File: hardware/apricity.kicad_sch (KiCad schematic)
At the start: 2 parts

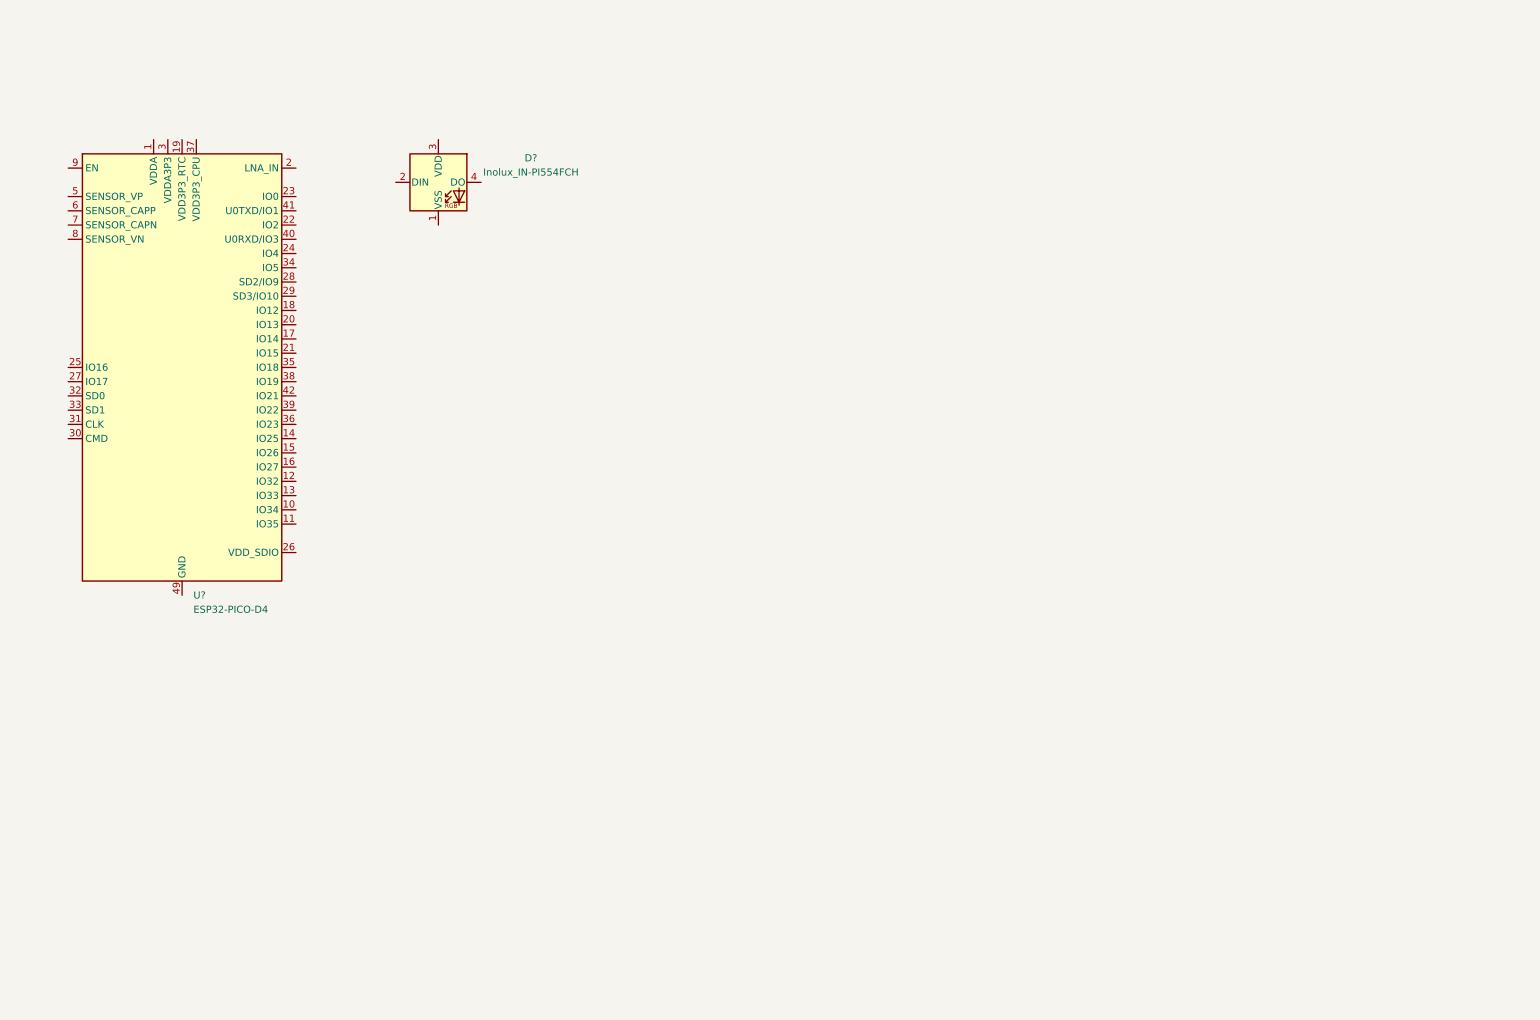
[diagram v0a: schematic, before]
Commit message: Prototype ESP8266-based version
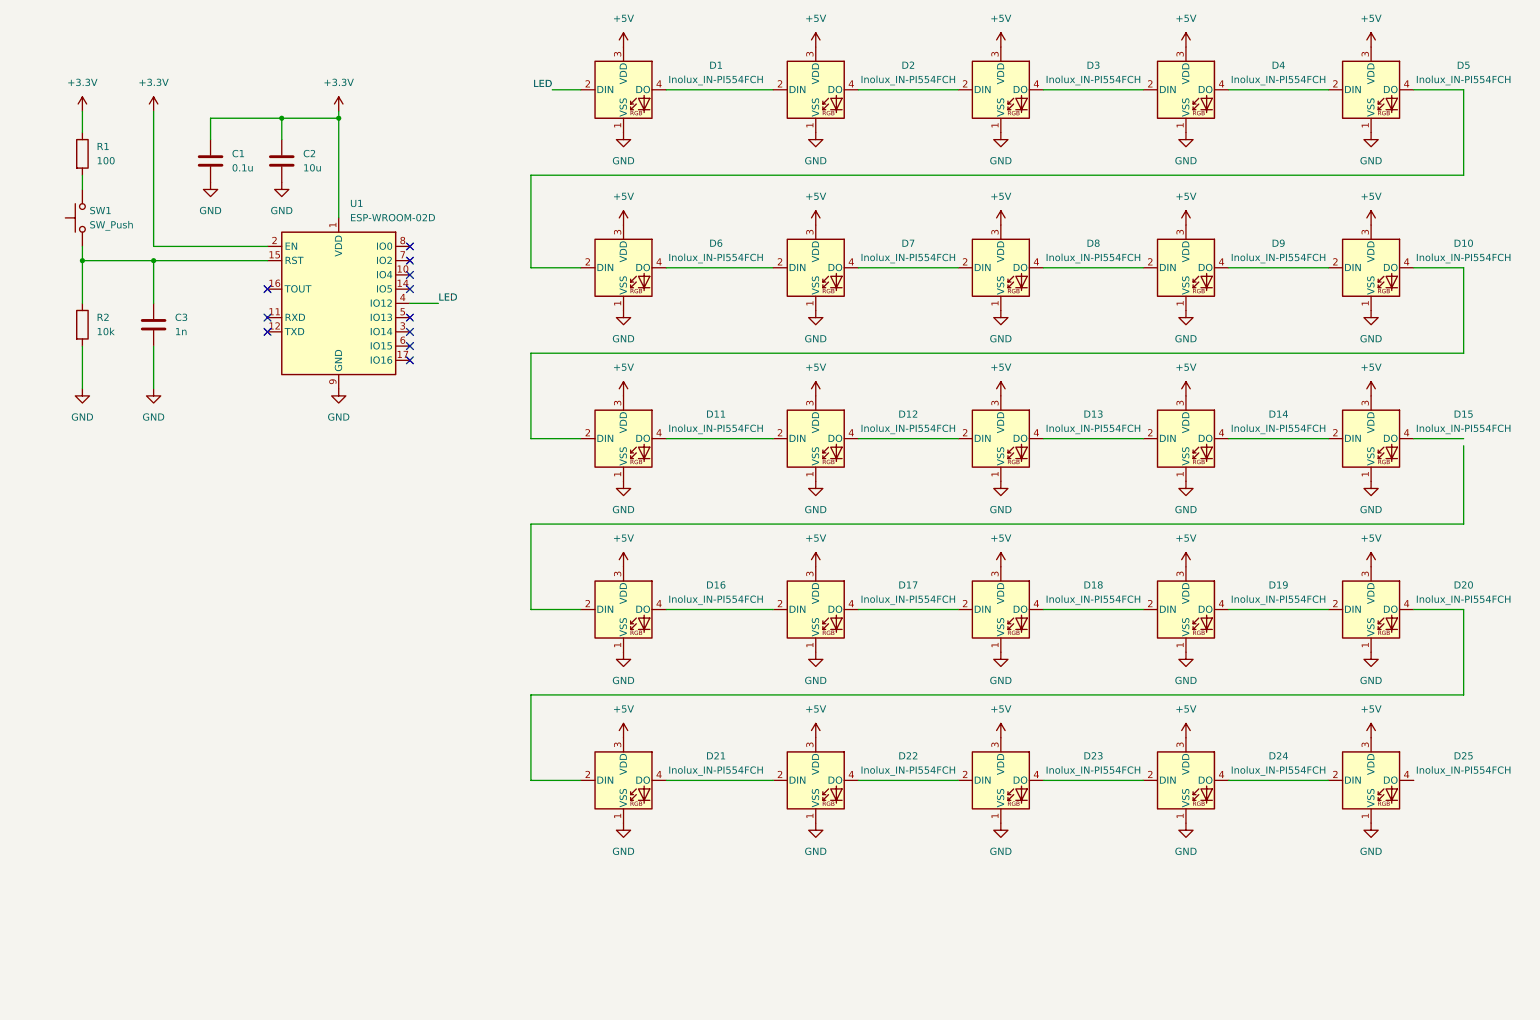
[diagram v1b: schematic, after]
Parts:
- removed U?: ESP32-PICO-D4, Package_DFN_QFN:QFN-48-1EP_7x7mm_P0.5mm_EP5.3x5.3mm, symbol RF_Module:ESP32-PICO-D4
- added C1: 0.1u, symbol Device:C
- added C2: 10u, symbol Device:C
- added C3: 1n, symbol Device:C
- added D1, D10, D11, D12, D13, D14, D15, D16, D17, D18, D19, D20, D21, D22, D23, D24, D25, D3, D4, D5, D6, D7, D8, D9: Inolux_IN-PI554FCH, LED_SMD:LED_Inolux_IN-PI554FCH_PLCC4_5.0x5.0mm_P3.2mm, symbol LED:Inolux_IN-PI554FCH
- added R1: 100, Resistor_SMD:R_0805_2012Metric, symbol Device:R
- added R2: 10k, Resistor_SMD:R_0805_2012Metric, symbol Device:R
- added SW1: SW_Push, symbol Switch:SW_Push
- added U1: ESP-WROOM-02D, RF_Module:ESP-WROOM-02, symbol RF_Module:ESP-WROOM-02
- gave numbers to parts that had none: 1
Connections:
- net GND: now reaches D2.1 (VSS)
- net GND: now also C1.2, C2.2, C3.2, D1.1 (VSS), D10.1 (VSS), D11.1 (VSS), D12.1 (VSS), D13.1 (VSS), D14.1 (VSS), D15.1 (VSS), D16.1 (VSS), D17.1 (VSS), D18.1 (VSS), D19.1 (VSS), D20.1 (VSS), D21.1 (VSS), D22.1 (VSS), D23.1 (VSS), D24.1 (VSS), D25.1 (VSS), D3.1 (VSS), D4.1 (VSS), D5.1 (VSS), D6.1 (VSS), D7.1 (VSS), D8.1 (VSS), D9.1 (VSS), R2.2, U1.13 (GND), U1.18 (GND), U1.19 (GND), U1.9 (GND)
- net at D2.2 (DIN): now also D1.4 (DO)
- net +5V: now reaches D2.3 (VDD)
- net +5V: now also D1.3 (VDD), D10.3 (VDD), D11.3 (VDD), D12.3 (VDD), D13.3 (VDD), D14.3 (VDD), D15.3 (VDD), D16.3 (VDD), D17.3 (VDD), D18.3 (VDD), D19.3 (VDD), D20.3 (VDD), D21.3 (VDD), D22.3 (VDD), D23.3 (VDD), D24.3 (VDD), D25.3 (VDD), D3.3 (VDD), D4.3 (VDD), D5.3 (VDD), D6.3 (VDD), D7.3 (VDD), D8.3 (VDD), D9.3 (VDD)
- net at D2.4 (DO): now also D3.2 (DIN)
- new net: D16.4 (DO), D17.2 (DIN)
- new net: D17.4 (DO), D18.2 (DIN)
- new net: C3.1, R2.1, SW1.1, U1.15 (RST)
- new net: D22.4 (DO), D23.2 (DIN)
- new net: D23.4 (DO), D24.2 (DIN)
- new net: R1.2, SW1.2
- new net: D13.4 (DO), D14.2 (DIN)
- new net: D14.4 (DO), D15.2 (DIN)
- new net: D24.4 (DO), D25.2 (DIN)
- new net: D12.4 (DO), D13.2 (DIN)
- new net: D18.4 (DO), D19.2 (DIN)
- new net: D10.4 (DO), D11.2 (DIN)
- new net: D11.4 (DO), D12.2 (DIN)
- new net: D19.4 (DO), D20.2 (DIN)
- new net: D3.4 (DO), D4.2 (DIN)
- new net: D4.4 (DO), D5.2 (DIN)
- new net: D7.4 (DO), D8.2 (DIN)
- new net: D8.4 (DO), D9.2 (DIN)
- new net: D6.4 (DO), D7.2 (DIN)
- new net: D20.4 (DO), D21.2 (DIN)
- new net: D5.4 (DO), D6.2 (DIN)
- new net: D10.2 (DIN), D9.4 (DO)
- new net: D21.4 (DO), D22.2 (DIN)
- new net +3.3V: C1.1, C2.1, R1.1, U1.1 (VDD), U1.2 (EN)
- new net LED: D1.2 (DIN), U1.4 (IO12)
- no-connect marks 0 -> 11
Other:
- moved on the sheet: D2

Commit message: lay down prototype circular array
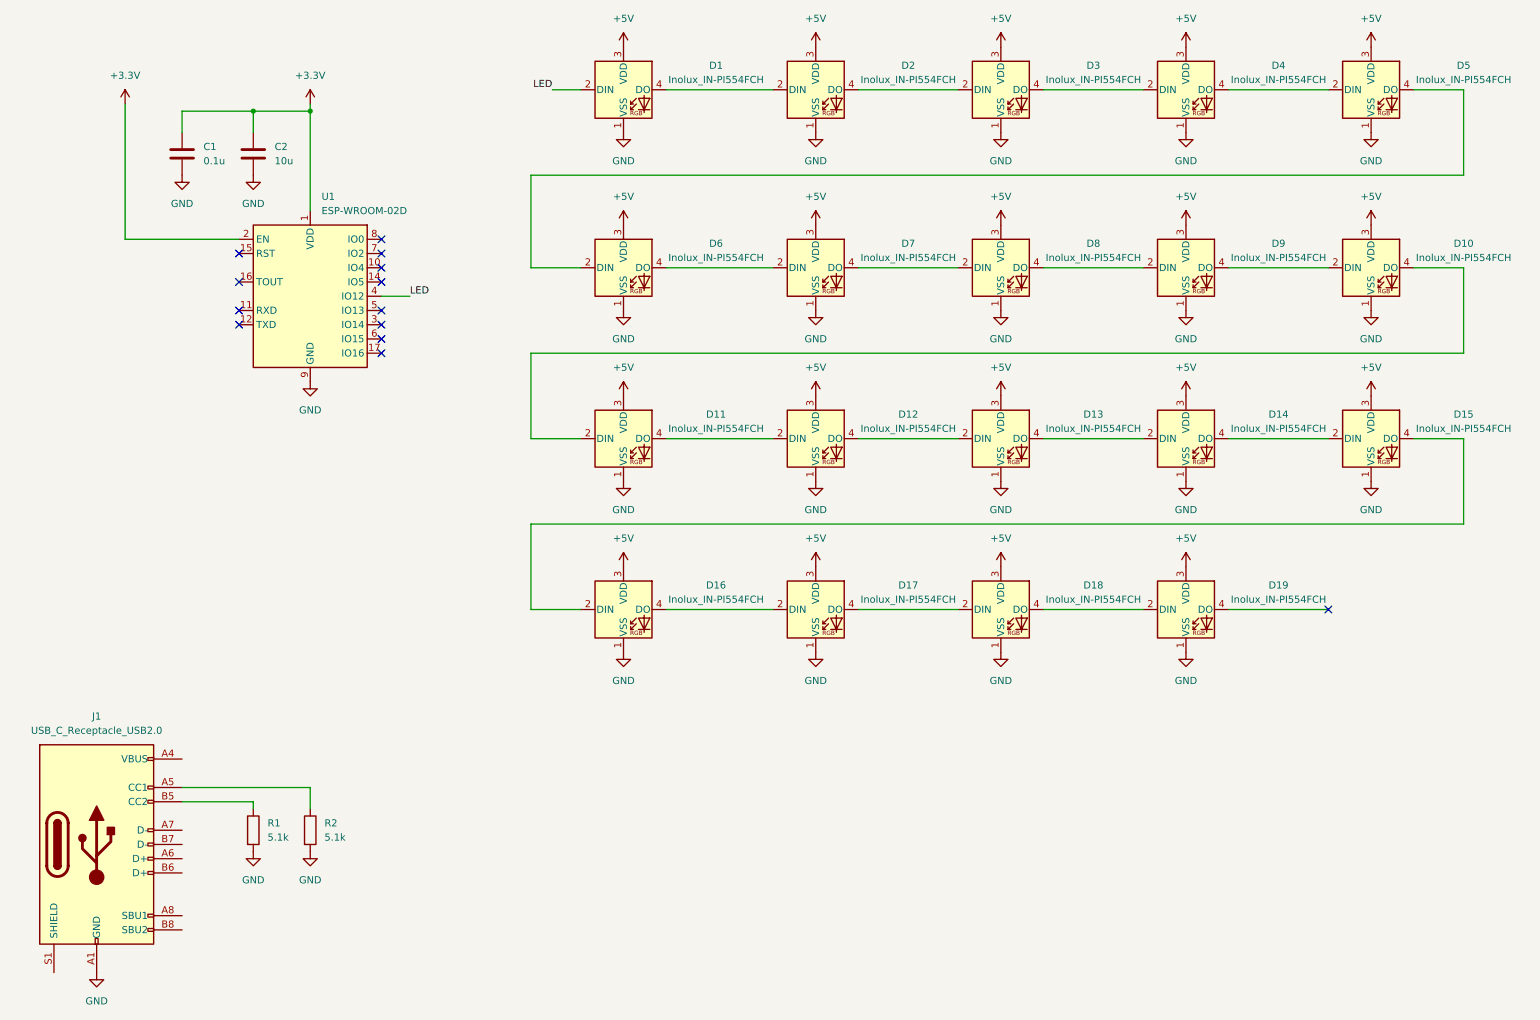
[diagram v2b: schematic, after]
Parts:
- removed C3: 1n, symbol Device:C
- removed D20, D21, D22, D23, D24, D25: Inolux_IN-PI554FCH, LED_SMD:LED_Inolux_IN-PI554FCH_PLCC4_5.0x5.0mm_P3.2mm, symbol LED:Inolux_IN-PI554FCH
- removed SW1: SW_Push, symbol Switch:SW_Push
- added J1: USB_C_Receptacle_USB2.0, Connector_USB:USB_C_Receptacle_GCT_USB4085, symbol Connector:USB_C_Receptacle_USB2.0
- R1: value 100 -> 5.1k; footprint Resistor_SMD:R_0805_2012Metric -> (none)
- R2: value 10k -> 5.1k; footprint Resistor_SMD:R_0805_2012Metric -> (none)
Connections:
- net +3.3V: no longer R1.1
- net GND: now also R1.2, J1.A1 (GND), J1.A12 (GND), J1.B1 (GND), J1.B12 (GND)
- net at U1.15 (RST): no longer R2.1
- net at D15.4 (DO): now also D16.2 (DIN)
- new net: J1.B5 (CC2), R1.1
- new net: J1.A5 (CC1), R2.1
- new net: J1.A4 (VBUS), J1.A9 (VBUS), J1.B4 (VBUS), J1.B9 (VBUS)
- no-connect marks 11 -> 13
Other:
- moved on the sheet: C1, C2, U1

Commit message: Annotate schematic and add power components
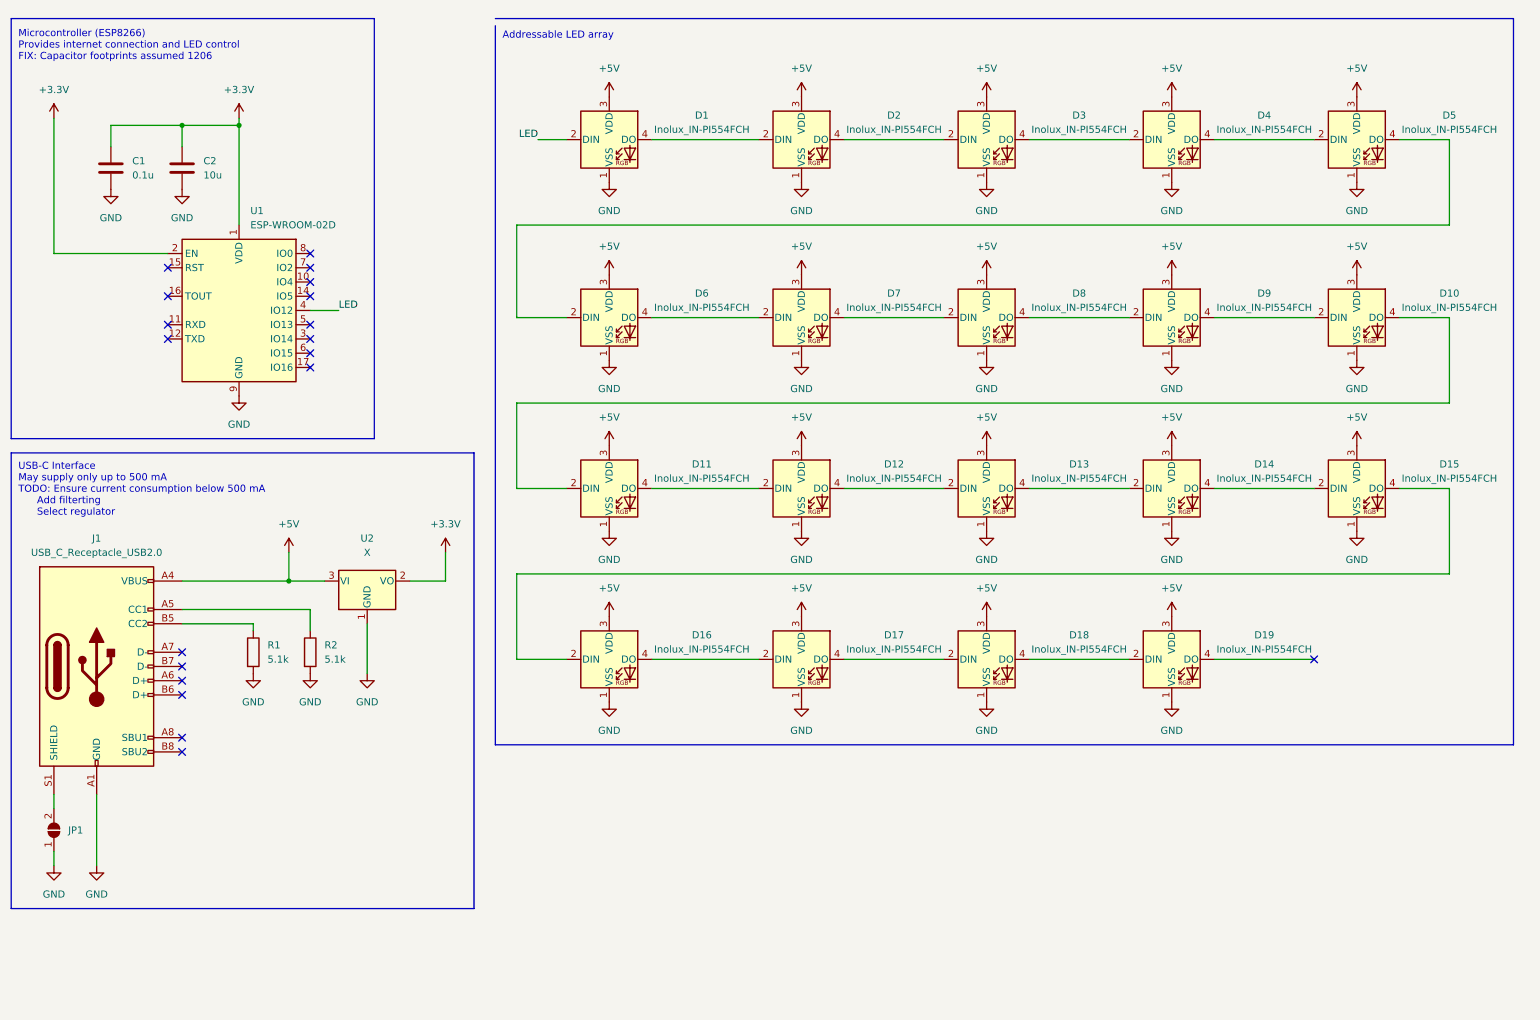
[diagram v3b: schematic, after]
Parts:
- added JP1: SolderJumper_2_Open, symbol Jumper:SolderJumper_2_Open
- added U2: X, Package_TO_SOT_SMD:TSOT-23_HandSoldering, symbol Regulator_Linear:AMS1117-3.3
- C1, C2: footprint (none) -> Capacitor_SMD:C_1206_3216Metric
- R1, R2: footprint (none) -> Resistor_SMD:R_0805_2012Metric
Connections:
- net +3.3V: now also U2.2 (VO)
- net +5V: now also J1.A4 (VBUS), J1.A9 (VBUS), J1.B4 (VBUS), J1.B9 (VBUS), U2.3 (VI)
- net GND: now also JP1.1 (A), U2.1 (GND)
- net at J1.S1 (SHIELD): now also JP1.2 (B)
- no-connect marks 13 -> 19
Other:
- note added: "Addressable LED array"
- note added: "Microcontroller (ESP8266) Provides internet connection and LED control FIX: Capacitor footprints assumed 1206"
- note added: "USB-C Interface May supply only up to 500 mA TODO: Ensure current consumption below 500 mA Add filterting Select regulator"
- moved on the sheet: C1, C2, D1, D10, D11, D12, D13, D15, D16, D17, D18, D19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

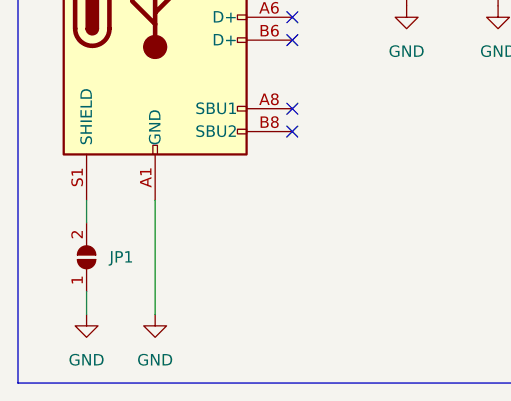
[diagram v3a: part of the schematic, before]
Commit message: layout power components on pcb
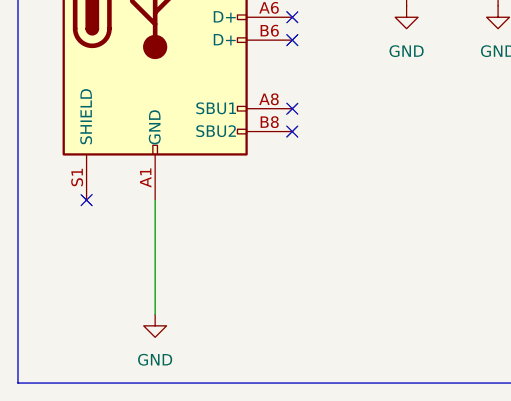
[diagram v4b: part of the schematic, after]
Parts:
- removed JP1: SolderJumper_2_Open, symbol Jumper:SolderJumper_2_Open
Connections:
- no-connect marks 19 -> 20
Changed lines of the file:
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@@
   )
   (no_connect (at 45.72 143.51))
+  (no_connect (at 22.86 153.67))
   (no_connect (at 68.58 77.47))
   (no_connect (at 68.58 64.77))
@@
   (no_connect (at 45.72 135.89))
   (no_connect (at 68.58 69.85))
-  (wire (pts (xy 22.86 163.83) (xy 22.86 166.37))
-    (stroke (width 0) (type default) (color 0 0 0 0))
-  )
   (wire (pts (xy 229.87 68.58) (xy 247.65 68.58))
     (stroke (width 0) (type default) (color 0 0 0 0))
@@
   )
   (wire (pts (xy 105.41 129.54) (xy 114.3 129.54))
-    (stroke (width 0) (type default) (color 0 0 0 0))
-  )
-  (wire (pts (xy 22.86 153.67) (xy 22.86 156.21))
     (stroke (width 0) (type default) (color 0 0 0 0))
   )
@@
     (pin "1")
   )
-  (symbol (lib_id "power:GND") (at 22.86 166.37 0) (unit 1)
-    (in_bom yes) (on_board yes) (fields_autoplaced)
-    (property "Reference" "#PWR049" (id 0) (at 22.86 172.72 0)
-      (effects (font (size 1.27 1.27)) hide)
-    )
-    (property "Value" "GND" (id 1) (at 22.86 171.45 0))
-    (property "Footprint" "" (id 2) (at 22.86 166.37 0)
-      (effects (font (size 1.27 1.27)) hide)
-    )
-    (property "Datasheet" "" (id 3) (at 22.86 166.37 0)
-      (effects (font (size 1.27 1.27)) hide)
-    )
-    (pin "1")
-  )
   (symbol (lib_id "power:+5V") (at 156.21 29.21 0) (unit 1)
     (in_bom yes) (on_board yes) (fields_autoplaced)
@@
     )
     (pin "1")
-  )
-  (symbol (lib_id "Jumper:SolderJumper_2_Open") (at 22.86 160.02 90) (unit 1)
-    (in_bom yes) (on_board yes) (fields_autoplaced)
-    (property "Reference" "JP1" (id 0) (at 25.4 160.0199 90)
-      (effects (font (size 1.27 1.27)) (justify right))
-    )
-    (property "Value" "SolderJumper_2_Open" (id 1) (at 25.4 161.2899 90)
-      (effects (font (size 1.27 1.27)) (justify right) hide)
-    )
-    (property "Footprint" "" (id 2) (at 22.86 160.02 0)
-      (effects (font (size 1.27 1.27)) hide)
-    )
-    (property "Datasheet" "~" (id 3) (at 22.86 160.02 0)
-      (effects (font (size 1.27 1.27)) hide)
-    )
-    (pin "1")
-    (pin "2")
   )
   (symbol (lib_id "power:+5V") (at 156.21 121.92 0) (unit 1)
@@
       (reference "#PWR048") (unit 1) (value "GND") (footprint "")
     )
-    (path "/8088c610-75e5-445a-810f-db520c1a5a91"
-      (reference "#PWR049") (unit 1) (value "GND") (footprint "")
-    )
     (path "/e2c4a6fe-1e37-465a-8920-4c4fc7446705"
       (reference "#PWR050") (unit 1) (value "GND") (footprint "")
@@
       (reference "J1") (unit 1) (value "USB_C_Receptacle_USB2.0") (footprint "Connector_USB:USB_C_Receptacle_GCT_USB4085")
     )
-    (path "/91d1ca4e-50dd-4a51-8711-673ec4693390"
-      (reference "JP1") (unit 1) (value "SolderJumper_2_Open") (footprint "")
-    )
     (path "/0d05b2dd-0847-494b-a812-c82d7fd47262"

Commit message: Play with power planes
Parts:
- J1: footprint Connector_USB:USB_C_Receptacle_GCT_USB4085 -> Connector_USB:USB_C_Receptacle_XKB_U262-16XN-4BVC11
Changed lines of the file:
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@@
     (property "Reference" "J1" (id 0) (at 30.48 107.95 0))
     (property "Value" "USB_C_Receptacle_USB2.0" (id 1) (at 30.48 110.49 0))
-    (property "Footprint" "Connector_USB:USB_C_Receptacle_GCT_USB4085" (id 2) (at 34.29 130.81 0)
+    (property "Footprint" "Connector_USB:USB_C_Receptacle_XKB_U262-16XN-4BVC11" (id 2) (at 34.29 130.81 0)
       (effects (font (size 1.27 1.27)) hide)
     )
@@
     )
     (path "/efec80d5-3b93-449b-967c-e6308c2f145f"
-      (reference "J1") (unit 1) (value "USB_C_Receptacle_USB2.0") (footprint "Connector_USB:USB_C_Receptacle_GCT_USB4085")
+      (reference "J1") (unit 1) (value "USB_C_Receptacle_USB2.0") (footprint "Connector_USB:USB_C_Receptacle_XKB_U262-16XN-4BVC11")
     )
     (path "/0d05b2dd-0847-494b-a812-c82d7fd47262"
